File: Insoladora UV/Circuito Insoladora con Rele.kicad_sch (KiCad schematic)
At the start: 34 parts, among them J1 Entrada 5V/2A, J2 RELE1, J3 RELE2, K1 SANYOU_SRD_Form_C, K2 SANYOU_SRD_Form_C, Q1 BC548, Q2 BC548, SW1 RESET, SW2 UP, SW3 DOWN, SW4 START/STOP, U1 PIC16F886-IP, U2 PC817, U3 PC817

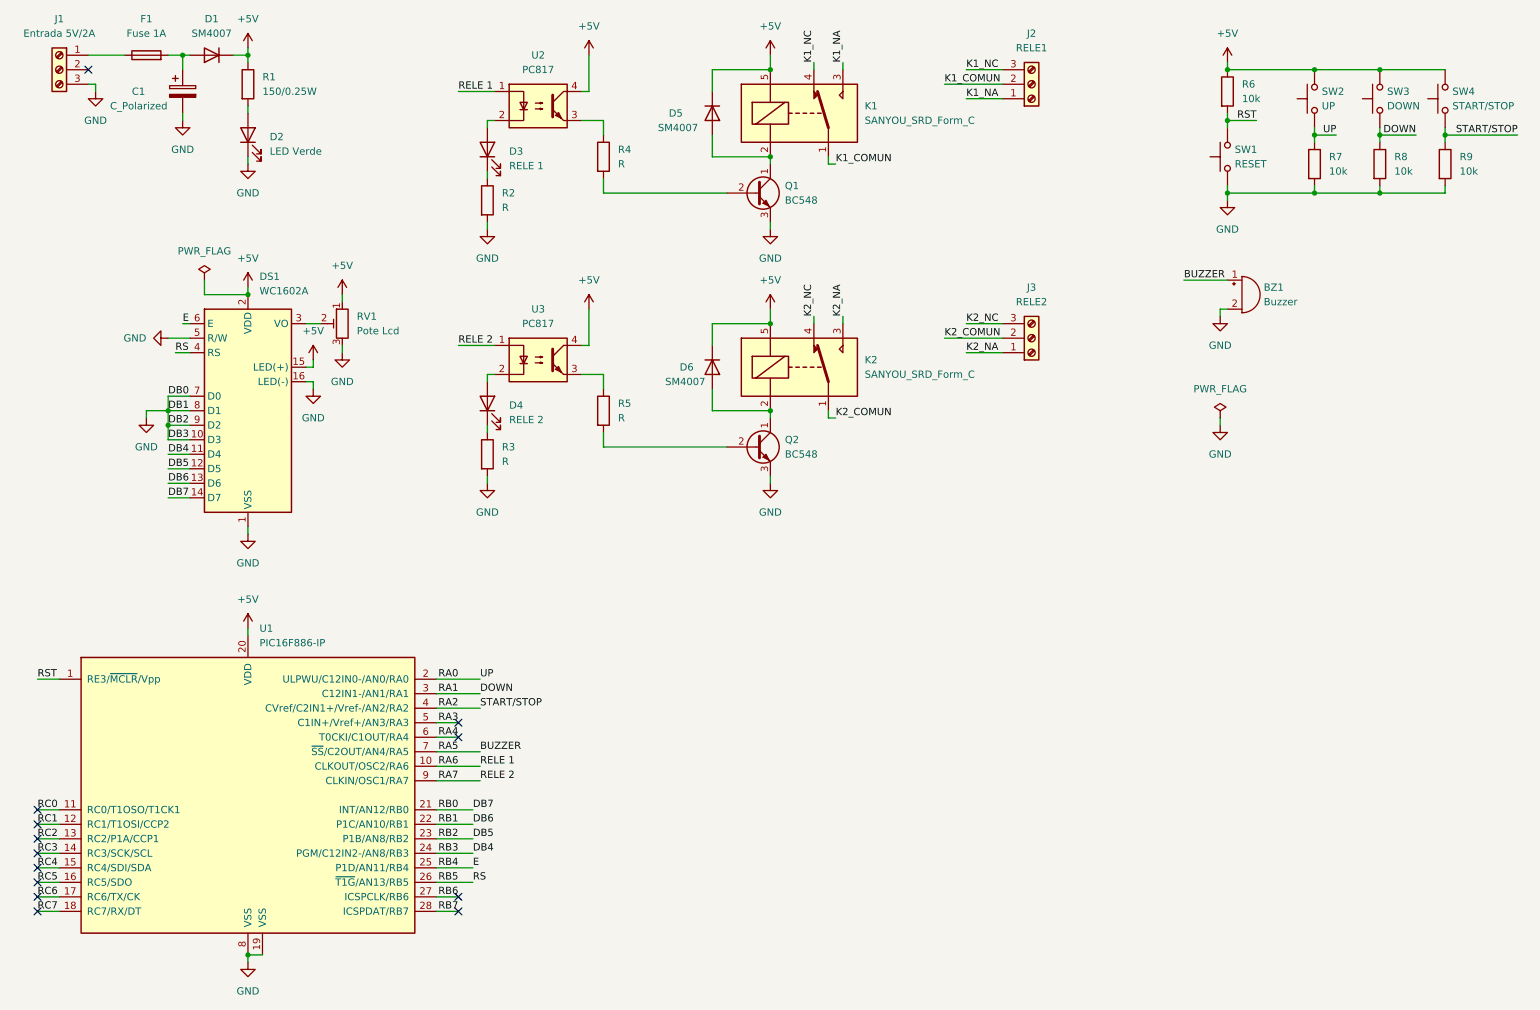
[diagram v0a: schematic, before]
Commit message: Insoladora
Se termino la pcb de 10x10 para la insoladora
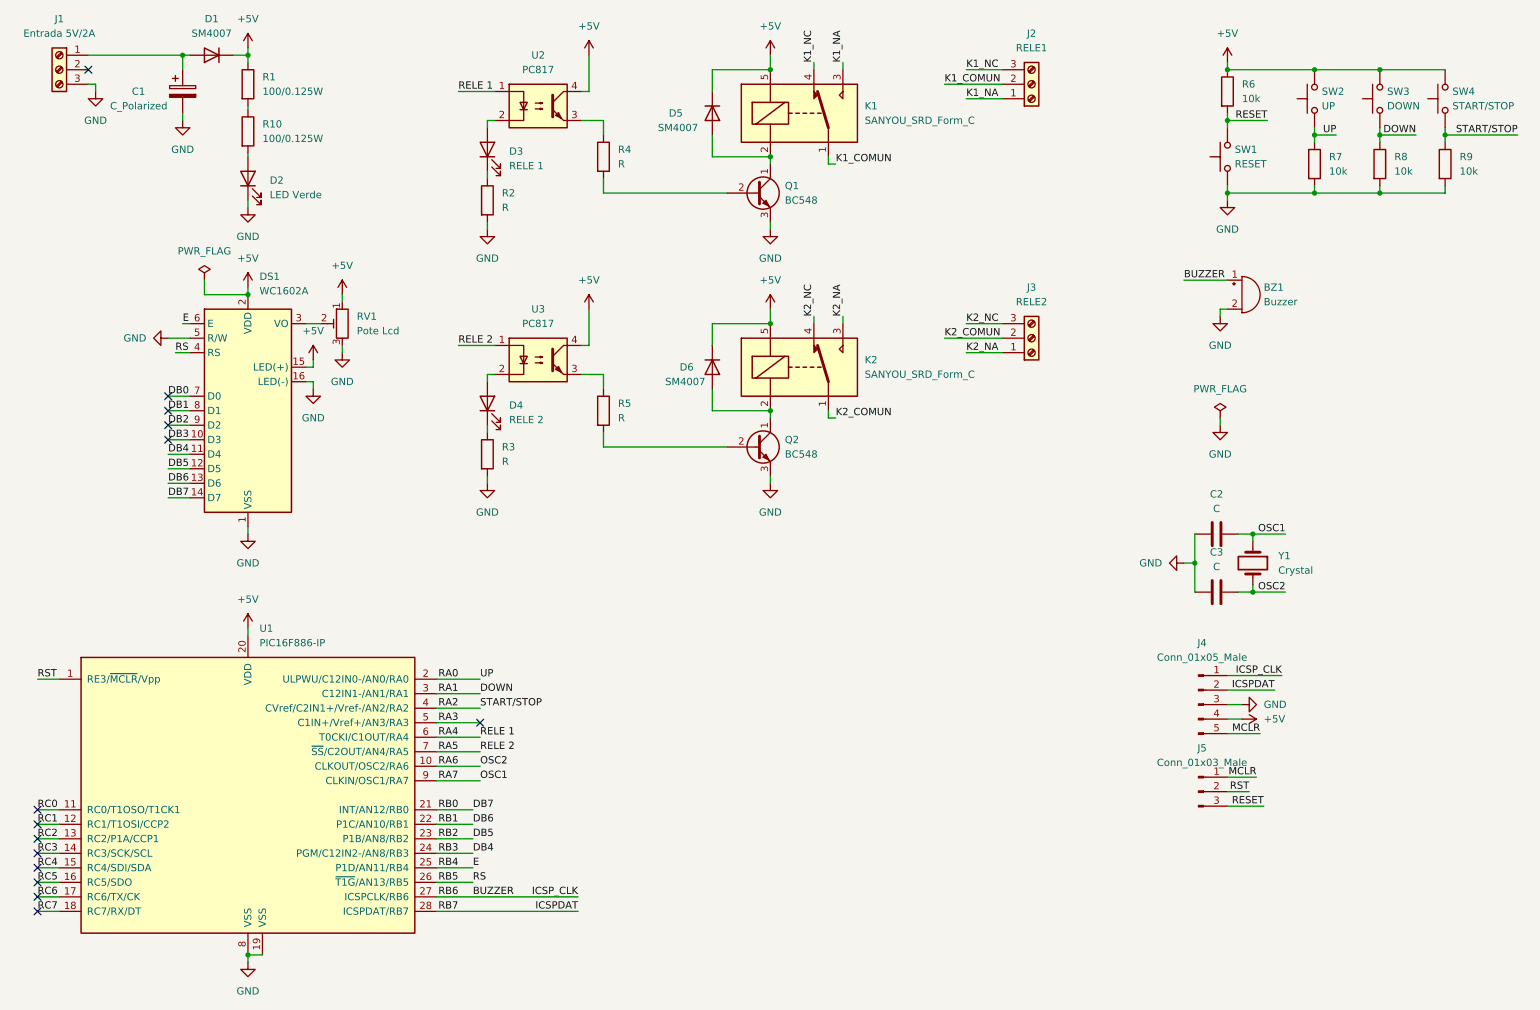
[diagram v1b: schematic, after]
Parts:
- removed F1: Fuse 1A, symbol Device:Fuse
- added C2, C3: C, Capacitor_THT:C_Disc_D4.7mm_W2.5mm_P5.00mm, symbol Device:C
- added J4: Conn_01x05_Male, Connector_PinHeader_2.54mm:PinHeader_1x05_P2.54mm_Vertical, symbol Connector:Conn_01x05_Male
- added J5: Conn_01x03_Male, Connector_PinHeader_2.54mm:PinHeader_1x03_P2.54mm_Vertical, symbol Connector:Conn_01x03_Male
- added R10: 100/0.125W, Resistor_SMD:R_0805_2012Metric, symbol Device:R
- added Y1: Crystal, Crystal:Crystal_HC52-8mm_Vertical, symbol Device:Crystal
- D2: footprint LED_THT:LED_D5.0mm -> LED_SMD:LED_0805_2012Metric
- R1: value 150/0.25W -> 100/0.125W; footprint Resistor_THT:R_Axial_DIN0207_L6.3mm_D2.5mm_P10.16mm_Horizontal -> Resistor_SMD:R_0805_2012Metric
- R6, R7, R8, R9: footprint Resistor_THT:R_Axial_DIN0207_L6.3mm_D2.5mm_P10.16mm_Horizontal -> Resistor_SMD:R_0805_2012Metric
- U2, U3: footprint Package_DIP:DIP-4_W7.62mm -> Package_DIP:DIP-4_W7.62mm_LongPads
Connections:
- net RB6 is gone; now on net BUZZER: U1.27 (ICSPCLK/RB6)
- net +5V: now also J4.4 (Pin_4)
- net BUZZER: now also J4.1 (Pin_1); no longer U1.7 (~{SS}/C2OUT/AN4/RA5)
- net GND: now also C2.1, C3.1, J4.3 (Pin_3); no longer DS1.10 (D3), DS1.7 (D0), DS1.8 (D1), DS1.9 (D2)
- net RA4: now also U2.1
- net RST: now also J5.2 (Pin_2); no longer R6.2, SW1.2
- net at R1.2: now also R10.1; no longer D2.2 (A)
- net at J1.1 (Pin_1): now also C1.1, D1.2 (A)
- net RA6 renamed OSC2
- net OSC2: now also C3.2, Y1.2; no longer U2.1
- net RA7 renamed OSC1
- net OSC1: now also C2.2, Y1.1; no longer U3.1
- net RB7 renamed ICSPDAT
- net ICSPDAT: now also J4.2 (Pin_2)
- new net: D2.2 (A), R10.2
- new net DB0: DS1.7 (D0)
- new net DB1: DS1.8 (D1)
- new net DB2: DS1.9 (D2)
- new net DB3: DS1.10 (D3)
- new net MCLR: J4.5 (Pin_5), J5.1 (Pin_1)
- new net RA5: U1.7 (~{SS}/C2OUT/AN4/RA5), U3.1
- new net RESET: J5.3 (Pin_3), R6.2, SW1.2
- no-connect marks 13 -> 14
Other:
- moved on the sheet: D2
